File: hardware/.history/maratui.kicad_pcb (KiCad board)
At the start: 2 copper layers, 109 x 55 mm, 6 parts, among them J1 Power Supply, J2 Lelit Mara, SW1 Button, U1 Ili9341_TFT_320x240

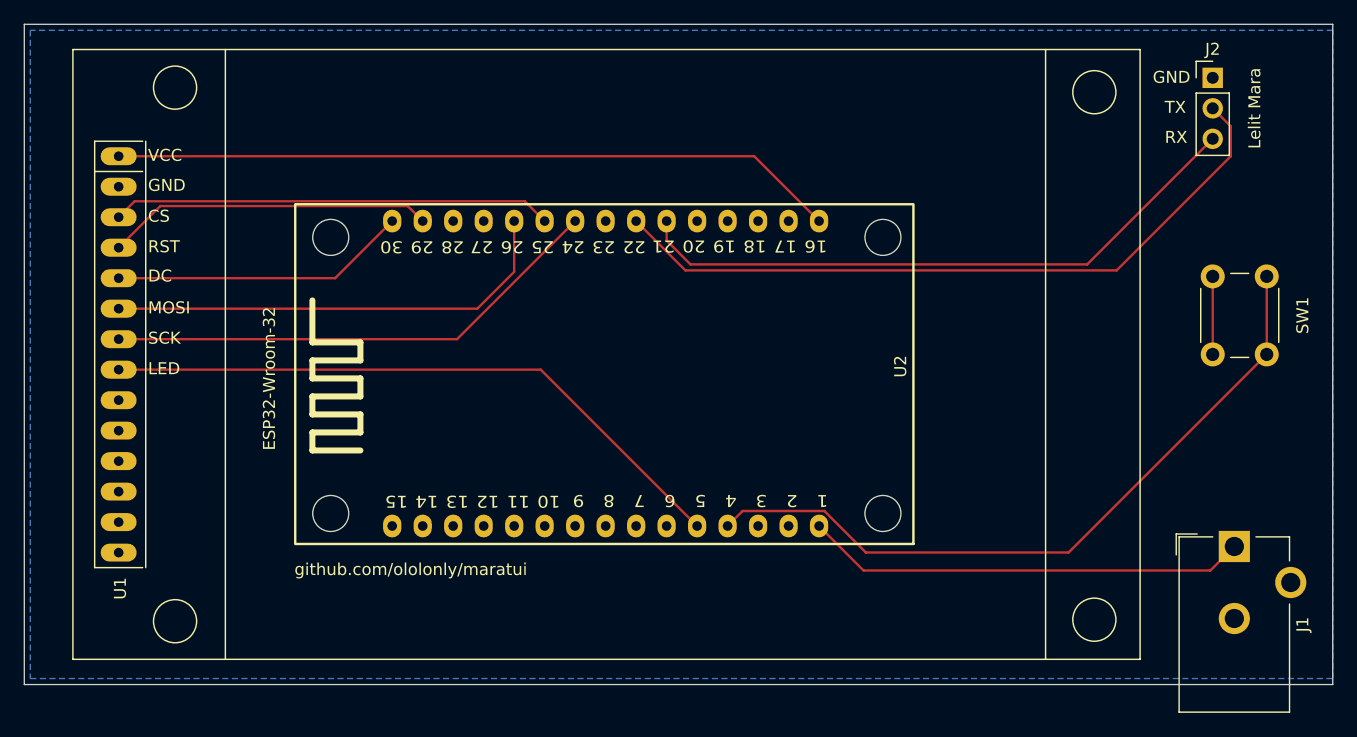
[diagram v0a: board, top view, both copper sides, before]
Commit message: feat(hardware): scale-integrated board revision, 3D-printed scale mount
- Replace the board design (schematic, PCB, gerbers, .step) with the
  newer revision that includes the HX711 scale sockets — the previous
  files predated the scale feature entirely and no longer matched the
  firmware.
- Add hardware/lib/footprints/maratui.pretty/HX711_Socket.kicad_mod.
- Add hardware/3d-print/: printable case parts for the dual load-cell
  mount (doppelfuss = double foot, auflage_v2 = scale platform) as
  STEP/STL plus pre-sliced G-code.
- hardware/README.md: HX711 wiring table, 3s-hold calibration note, and
  a 3D-Printed Parts section; drop the stale gerbers/maratui-v1.zip
  reference in favor of the current gerbers.zip (base board) and
  260903_Platine_waage.zip (scale add-on board).

Co-Authored-By: Claude Sonnet 5 <noreply@anthropic.com>
Claude-Session: https://claude.ai/code/session_01Ko6obK5yneSFLNZKCRo7FE
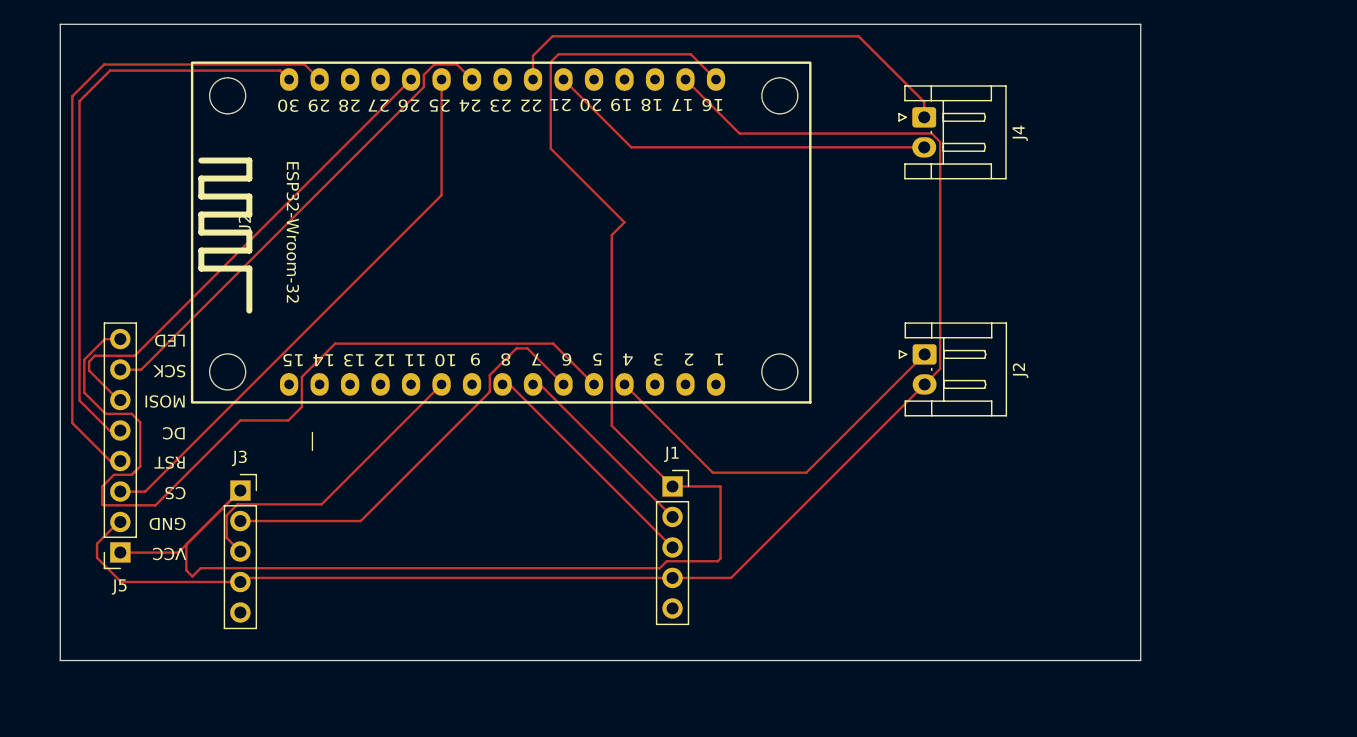
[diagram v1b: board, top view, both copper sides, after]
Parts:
- removed G***: LOGO, LOGO
- removed SW1: Button, Button_Switch_THT:SW_PUSH_6mm
- removed U1: Ili9341_TFT_320x240, Maratui Footprints:TFT-320x240
- added J3: Conn_01x04_Socket, Connector_PinSocket_2.54mm:PinSocket_1x05_P2.54mm_Vertical, F.Cu at (99.5, 87.3)
- added J4: Conn_01x02_Socket, Connector_JST:JST_EH_S2B-EH_1x02_P2.50mm_Horizontal, F.Cu at (156.5, 56.2)
- added J5: Conn_01x08_Socket, Connector_PinSocket_2.54mm:PinSocket_1x08_P2.54mm_Vertical, F.Cu at (89.5, 92.5)
- J1: value Power Supply -> Conn_01x04_Socket; footprint Connector_BarrelJack:BarrelJack_CUI_PJ-102AH_Horizontal -> Connector_PinSocket_2.54mm:PinSocket_1x05_P2.54mm_Vertical
- J2: value Lelit Mara -> Button; footprint Connector_PinHeader_2.54mm:PinHeader_1x03_P2.54mm_Vertical -> Connector_JST:JST_EH_S2B-EH_1x02_P2.50mm_Horizontal
- moved J1 47.1 mm to (135.5, 87.0)
- moved J2 33.3 mm to (156.5, 76.0), turned to -90 degrees
- moved U2 14.6 mm to (121.6, 66.0)
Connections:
- J1 pad 1: +5V -> +3.3V
- J1 pad 2: GND -> SCK_26
- J1 pad 3: (no net) -> Dat_25
- J2 pad 1: GND -> /BUTTON
- J2 pad 2: Net-(J2-Pin_2) -> GND
- U2 pad 10: unconnected-(U2-GPIO32-Pad10) -> Dat_32
- U2 pad 21: Net-(J2-Pin_3) -> Net-(J4-Pin_2)
- U2 pad 22: Net-(J2-Pin_2) -> Net-(J4-Pin_1)
- U2 pad 24: Net-(U1-SCK) -> sck_18
- U2 pad 25: Net-(U1-CS) -> cs_19
- U2 pad 26: Net-(U1-MOSI) -> Mosi_21
- U2 pad 30: Net-(U1-DC) -> DC_23
- U2 pad 6: unconnected-(U2-GPIO27-Pad6) -> SCK_27
- U2 pad 7: unconnected-(U2-GPIO26-Pad7) -> SCK_26
- U2 pad 8: unconnected-(U2-GPIO25-Pad8) -> Dat_25
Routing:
- net GND: track 6.50 -> 124.4 mm
- net +3.3V: track 60.6 -> 132.0 mm
- net Net-(J2-Pin_2): track 59.8 -> 0.00 mm
- net Net-(J2-Pin_3): track 52.3 -> 0.00 mm
- net DC_23: track 0.00 -> 48.1 mm
- net cs_19: track 0.00 -> 46.8 mm
- net Net-(U1-SCK): track 42.1 -> 0.00 mm
- net sck_18: track 0.00 -> 41.1 mm
- net Mosi_21: track 0.00 -> 40.8 mm
- net Net-(J4-Pin_1): track 0.00 -> 38.8 mm
- net Net-(U1-MOSI): track 38.4 -> 0.00 mm
- net +5V: track 37.0 -> 0.00 mm
- net Net-(U1-CS): track 36.7 -> 0.00 mm
- net SCK_27: track 0.00 -> 34.9 mm
- net Net-(J4-Pin_2): track 0.00 -> 32.4 mm
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- removed copper zone on B.Cu, net GND
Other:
- board size 109 x 55 mm -> 90 x 53 mm
- board text removed: "MARATUI"
- board text removed: "RX"
- board text removed: "TX"
- board text removed: "WORKS ON MY MACHINE VOID WARRANTY? ALREADY DONE. rm -rf /bad_shots && brew coffee"
- board text removed: "github.com/ololonly/maratui"
- board text removed: "https://github.com/ololonly/maratui"

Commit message: hardware: update PCB and gerbers for the ordered board revision
Updated schematic/PCB and regenerated gerbers.zip for the board
revision that was ordered from fab. Removed the now-superseded
separate scale add-on gerber zip (260903_Platine_waage.zip) — the
scale cells are part of the single-board gerbers.zip export.

Co-Authored-By: Claude Sonnet 5 <noreply@anthropic.com>
Claude-Session: https://claude.ai/code/session_01Ko6obK5yneSFLNZKCRo7FE
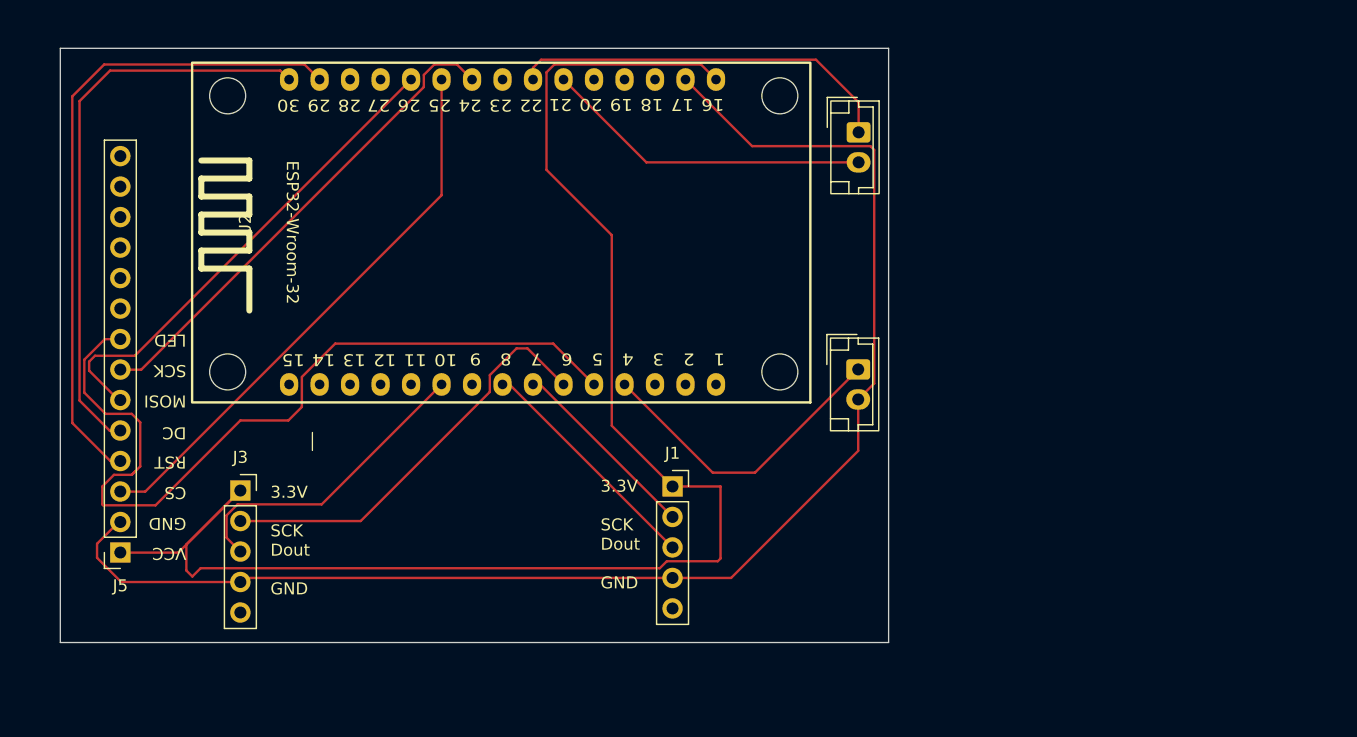
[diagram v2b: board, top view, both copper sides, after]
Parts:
- J1: value Conn_01x04_Socket -> Left
- J2: footprint Connector_JST:JST_EH_S2B-EH_1x02_P2.50mm_Horizontal -> Connector_JST:JST_EH_B2B-EH-A_1x02_P2.50mm_Vertical
- J3: value Conn_01x04_Socket -> Rigt
- J4: value Conn_01x02_Socket -> Mara; footprint Connector_JST:JST_EH_S2B-EH_1x02_P2.50mm_Horizontal -> Connector_JST:JST_EH_B2B-EH-A_1x02_P2.50mm_Vertical
- J5: value Conn_01x08_Socket -> TFT; footprint Connector_PinSocket_2.54mm:PinSocket_1x08_P2.54mm_Vertical -> Connector_PinSocket_2.54mm:PinSocket_1x14_P2.54mm_Vertical
- moved J2 5.67 mm to (151.0, 77.2)
- moved J4 5.61 mm to (151.0, 57.5)
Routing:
- net GND: track 124.4 -> 116.3 mm
- net Net-(J4-Pin_1): track 38.8 -> 32.3 mm
- net /BUTTON: track 32.1 -> 26.1 mm
- net Net-(J4-Pin_2): track 32.4 -> 27.4 mm
- net +3.3V: track 132.0 -> 130.4 mm
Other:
- board size 90 x 53 mm -> 69 x 49.5 mm
- board text added: "3.3V SCK Dout GND"
